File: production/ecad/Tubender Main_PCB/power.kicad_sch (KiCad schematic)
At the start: 61 parts, among them Q1 CSD19502Q5B, Q2 CSD19534Q5A, U1 LMR36520FADDAR, U11 LM5146RGYR, U13 LM5017SDX/NOPB, U3 MCP23017-E_SO

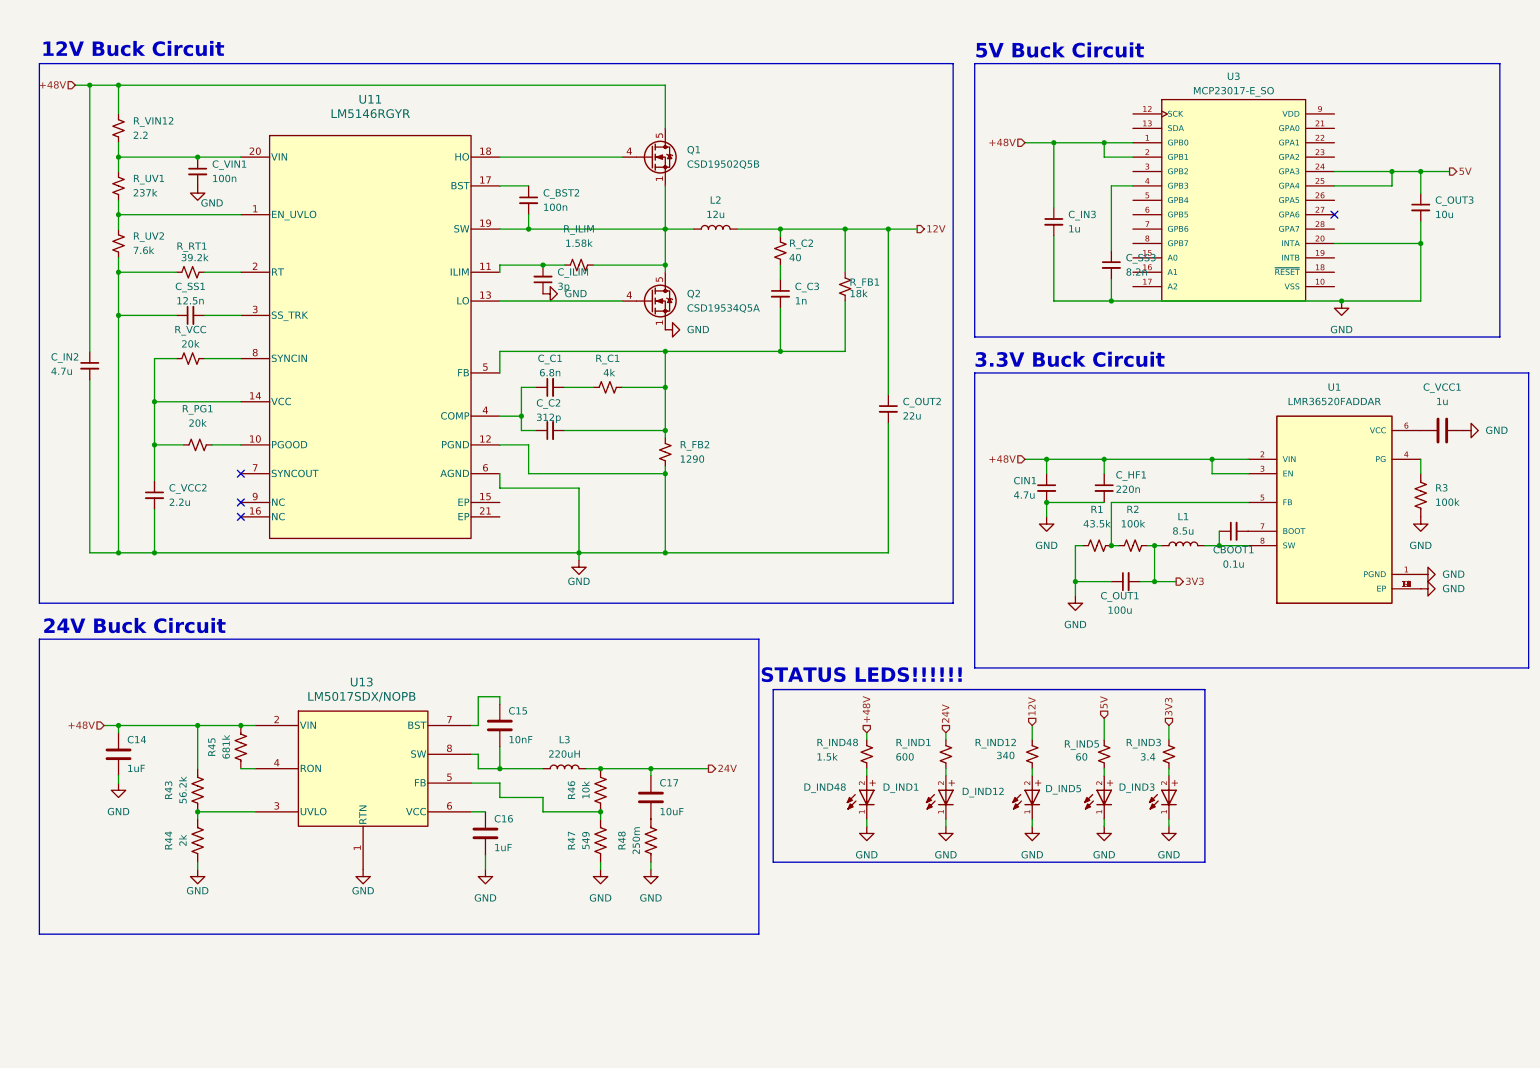
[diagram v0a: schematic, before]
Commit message: Fixed the Nets
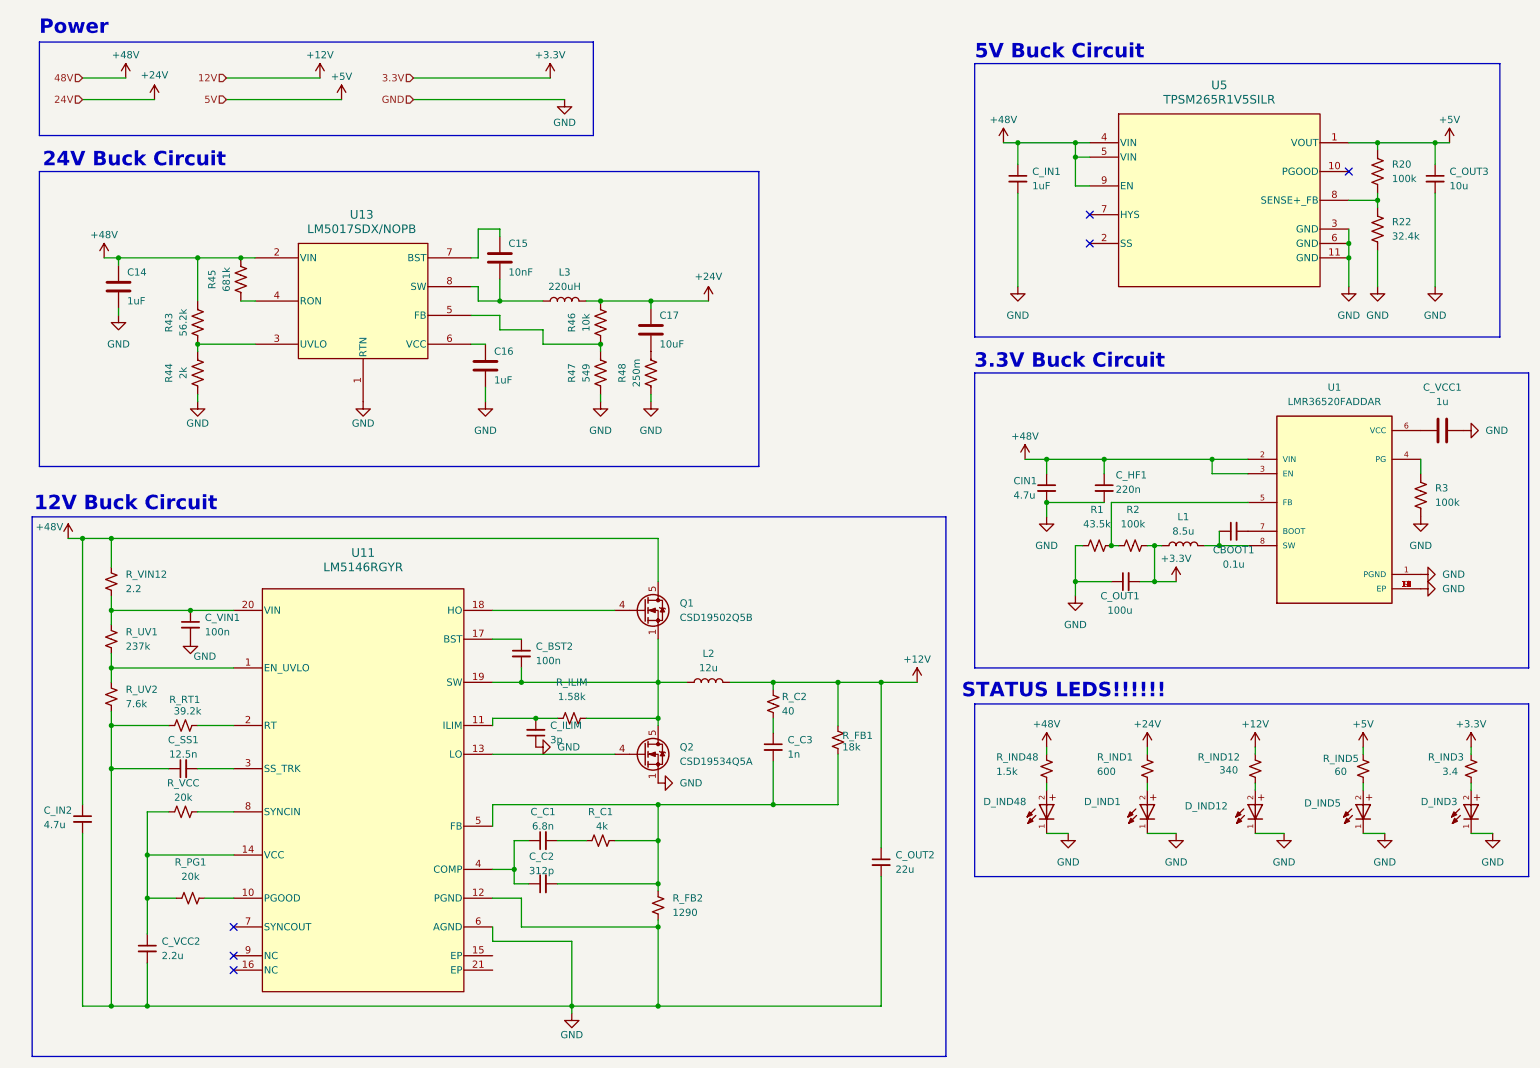
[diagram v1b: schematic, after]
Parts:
- removed C_IN3: 1u, symbol Device:C_Small
- removed C_SS3: 8.2n, symbol Device:C_Small
- removed U3: MCP23017-E_SO, MCP23017-E_SO:SOIC127P1030X265-28N, symbol TPSM265R1V5SILR:TPSM265R1V5SILR
- added C_IN1: 1uF, symbol Device:C_Small
- added R20: 100k, symbol Device:R_US
- added R22: 32.4k, symbol Device:R_US
- added U5: TPSM265R1V5SILR, SIL0010C, symbol 2024-10-15_18-36-57:TPSM265R1V5SILR
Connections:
- net +48V: now also C_IN1.1, U5.4 (VIN), U5.5 (VIN), U5.9 (EN)
- net GND: now also C_IN1.2, R22.1, U5.11 (GND), U5.3 (GND), U5.6 (GND)
- net 12V renamed +12V
- net 24V renamed +24V
- net 3V3 renamed +3.3V
- net 5V renamed +5V
- net +5V: now also R20.2, U5.1 (VOUT)
- new net: R20.1, R22.2, U5.8 (SENSE+_FB)
- no-connect marks 4 -> 6
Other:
- note added: "Power"
- moved on the sheet: C14, C15, C16, C17, C_BST2, C_C1, C_C2, C_C3, C_ILIM, C_IN2, C_OUT2, C_SS1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
